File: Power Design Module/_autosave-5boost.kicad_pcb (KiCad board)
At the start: 2 copper layers, 15 parts, among them J1 105430-1102, J2 105430-1102, J3 105430-1102, U1 TPS61232DRCR, U2 TPPM0110DWPR

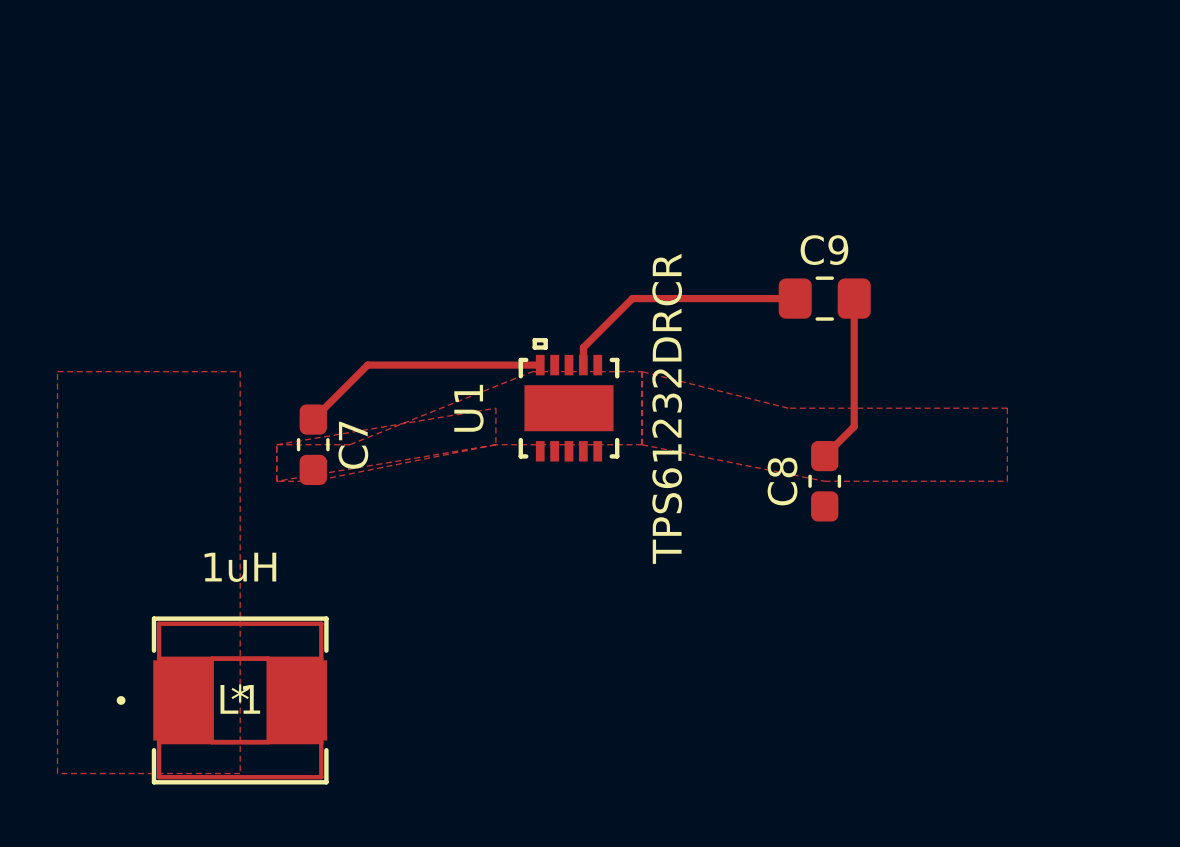
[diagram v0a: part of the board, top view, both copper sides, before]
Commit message: Layout and charging circuit progress.
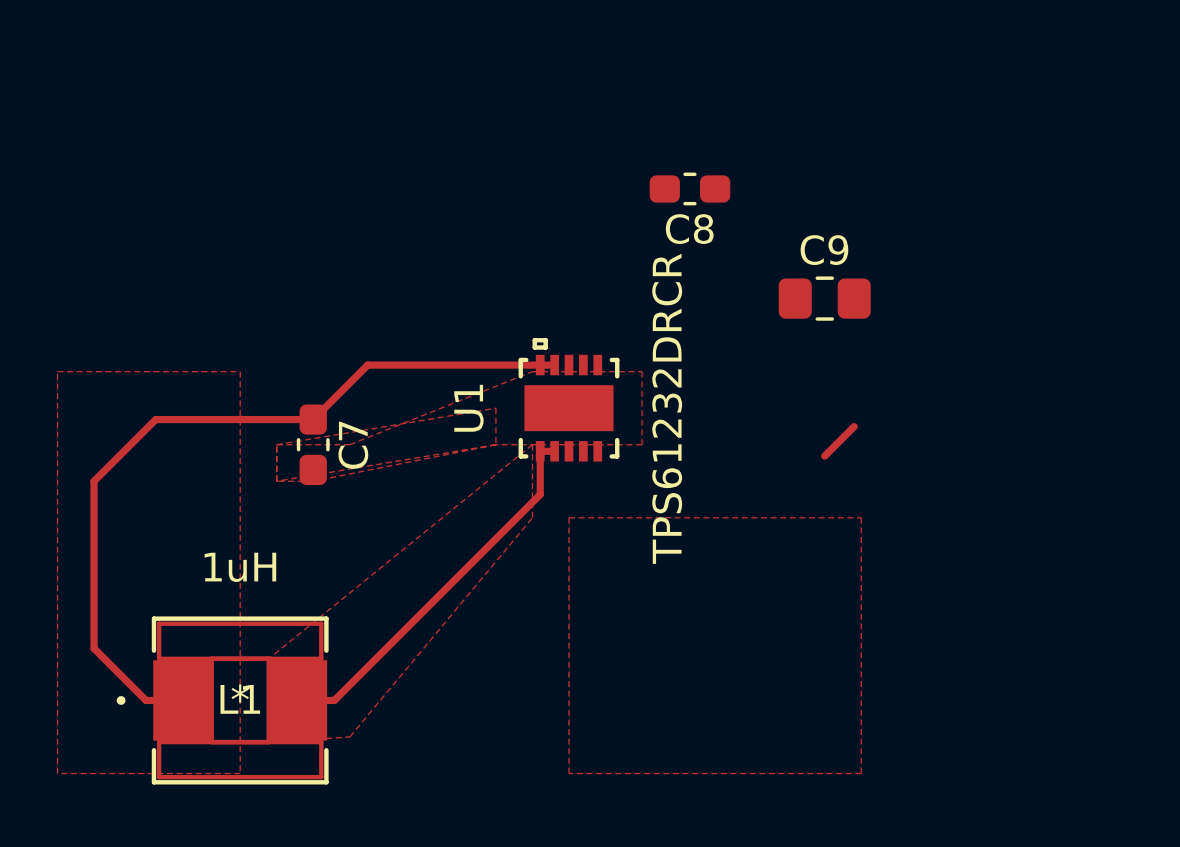
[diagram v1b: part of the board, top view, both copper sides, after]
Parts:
- moved C8 11.2 mm to (135.0, 82.5), turned to 180 degrees
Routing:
- net /ChargingCircuit/Voutbat: track 8.67 -> 27.3 mm
- net Net-(L1-Pad2): track 0.00 -> 13.4 mm
- net Net-(C1-Pad1): track 8.68 -> 0.00 mm
- net GND: track 5.90 -> 1.45 mm
- added copper zone on F.Cu, net Net-(C3-Pad1)
- added copper zone on F.Cu, net Net-(L1-Pad2)
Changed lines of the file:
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@@
     (thickness 1.6)
     (drawings 0)
-    (tracks 7)
+    (tracks 13)
     (zones 0)
     (modules 15)
@@
     (solder_mask_min_width 0.25)
     (aux_axis_origin 0 0)
-    (visible_elements FFFFFF7F)
+    (visible_elements 7FFFFFFF)
     (pcbplotparams
       (layerselection 0x010fc_ffffffff)
@@
   )
   (module Capacitor_SMD:C_0603_1608Metric_Pad1.05x0.95mm_HandSolder (layer F.Cu)
-    (at 139.7 92.71 90)
+    (at 135.015 82.55 180)
     (descr "Capacitor SMD 0603 (1608 Metric), square (rectangular) end terminal, IPC_7351 nominal with elongated pad for handsoldering. (Body size source: http://www.tortai-tech.com/upload/download/2011102023233369053.pdf), generated with kicad-footprint-generator")
     (tags "capacitor handsolder")
     (attr smd)
-    (fp_text reference C8 (at 0 -1.43 90) (layer F.SilkS)
-      (effects (font (size 1 1) (thickness 0.15)))
-    )
-    (fp_text value 15nF (at 0 1.43 90) (layer F.Fab)
-      (effects (font (size 1 1) (thickness 0.15)))
-    )
-    (fp_text user %R (at 0 0 90) (layer F.Fab)
+    (fp_text reference C8 (at 0 -1.43) (layer F.SilkS)
+      (effects (font (size 1 1) (thickness 0.15)))
+    )
+    (fp_text value 15nF (at 0 1.43) (layer F.Fab)
+      (effects (font (size 1 1) (thickness 0.15)))
+    )
+    (fp_text user %R (at 0 0) (layer F.Fab)
       (effects (font (size 0.4 0.4) (thickness 0.06)))
     )
@@
     (fp_line (start -0.8 -0.4) (end 0.8 -0.4) (layer F.Fab) (width 0.1))
     (fp_line (start -0.8 0.4) (end -0.8 -0.4) (layer F.Fab) (width 0.1))
-    (pad 2 smd roundrect (at 0.875 0 90) (size 1.05 0.95) (layers F.Cu F.Paste F.Mask) (roundrect_rratio 0.25)
-      (net 1 GND))
-    (pad 1 smd roundrect (at -0.875 0 90) (size 1.05 0.95) (layers F.Cu F.Paste F.Mask) (roundrect_rratio 0.25)
+    (pad 2 smd roundrect (at 0.875 0 180) (size 1.05 0.95) (layers F.Cu F.Paste F.Mask) (roundrect_rratio 0.25)
+      (net 1 GND))
+    (pad 1 smd roundrect (at -0.875 0 180) (size 1.05 0.95) (layers F.Cu F.Paste F.Mask) (roundrect_rratio 0.25)
       (net 6 "Net-(C8-Pad1)"))
     (model ${KISYS3DMOD}/Capacitor_SMD.3dshapes/C_0603_1608Metric.wrl
@@
   )
   (segment (start 140.725 90.81) (end 139.7 91.835) (width 0.25) (layer F.Cu) (net 1))
-  (segment (start 140.725 86.36) (end 140.725 90.81) (width 0.25) (layer F.Cu) (net 1))
-  (segment (start 131.309999 88.0658) (end 131.309999 88.6714) (width 0.25) (layer F.Cu) (net 2))
-  (segment (start 133.015799 86.36) (end 131.309999 88.0658) (width 0.25) (layer F.Cu) (net 2))
-  (segment (start 138.675 86.36) (end 133.015799 86.36) (width 0.25) (layer F.Cu) (net 2))
+  (segment (start 121.92 90.565) (end 123.8136 88.6714) (width 0.25) (layer F.Cu) (net 5))
   (segment (start 123.8136 88.6714) (end 129.809999 88.6714) (width 0.25) (layer F.Cu) (net 5))
-  (segment (start 121.92 90.565) (end 123.8136 88.6714) (width 0.25) (layer F.Cu) (net 5))
+  (segment (start 130.310001 88.6714) (end 129.809999 88.6714) (width 0.25) (layer F.Cu) (net 5))
+  (segment (start 121.92 90.565) (end 116.445 90.565) (width 0.25) (layer F.Cu) (net 5))
+  (segment (start 116.445 90.565) (end 114.3 92.71) (width 0.25) (layer F.Cu) (net 5))
+  (segment (start 116.1074 100.33) (end 117.348 100.33) (width 0.25) (layer F.Cu) (net 5))
+  (segment (start 114.3 98.5226) (end 116.1074 100.33) (width 0.25) (layer F.Cu) (net 5))
+  (segment (start 114.3 92.71) (end 114.3 98.5226) (width 0.25) (layer F.Cu) (net 5))
+  (segment (start 129.809999 93.172601) (end 129.809999 91.6686) (width 0.25) (layer F.Cu) (net 7))
+  (segment (start 121.412 100.33) (end 122.6526 100.33) (width 0.25) (layer F.Cu) (net 7))
+  (segment (start 122.6526 100.33) (end 129.809999 93.172601) (width 0.25) (layer F.Cu) (net 7))
+  (segment (start 129.809999 91.6686) (end 130.310001 91.6686) (width 0.25) (layer F.Cu) (net 7))
   (zone (net 1) (net_name GND) (layer F.Cu) (hatch edge 0.508)
     (connect_pads (clearance 0.508))
@@
     (polygon
       (pts
-        (xy 133.35 91.44) (xy 139.7 92.71) (xy 146.05 92.71) (xy 146.05 90.17) (xy 138.43 90.17)
-        (xy 133.35 88.9)
-      )
-    )
-  )
-  (zone (net 1) (net_name GND) (layer F.Cu) (hatch edge 0.508)
-    (connect_pads (clearance 0.508))
-    (min_thickness 0.254)
-    (fill yes (arc_segments 32) (thermal_gap 0.508) (thermal_bridge_width 0.508))
-    (polygon
-      (pts
         (xy 120.65 91.44) (xy 128.27 90.17) (xy 128.27 91.44) (xy 121.92 92.71) (xy 120.65 92.71)
       )
@@
       )
     )
+  )
+  (zone (net 3) (net_name "Net-(C3-Pad1)") (layer F.Cu) (hatch edge 0.508)
+    (connect_pads (clearance 0.508))
+    (min_thickness 0.254)
+    (fill yes (arc_segments 32) (thermal_gap 0.508) (thermal_bridge_width 0.508))
+    (polygon
+      (pts
+        (xy 130.81 93.98) (xy 140.97 93.98) (xy 140.97 102.87) (xy 130.81 102.87)
+      )
+    )
+  )
+  (zone (net 7) (net_name "Net-(L1-Pad2)") (layer F.Cu) (hatch edge 0.508)
+    (connect_pads (clearance 0.508))
+    (min_thickness 0.254)
+    (fill yes (arc_segments 32) (thermal_gap 0.508) (thermal_bridge_width 0.508))
+    (polygon
+      (pts
+        (xy 129.54 91.44) (xy 120.3706 98.8822) (xy 120.3706 101.7778) (xy 123.19 101.6) (xy 129.54 93.98)
+      )
+    )
